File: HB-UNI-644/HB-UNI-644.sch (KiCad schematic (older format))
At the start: 49 parts, among them J1 FTDI, J10 ICSP, J11 RAW, J12 Conn_Gnd, J13 Conn_NTC, J2 GS2, J3 I2C_1, J4 GS2, J5 I2C_2, J6 I2C_3, J7 I2C_4, J8 Conn_A, J9 Conn_B, Q1 IRLML6244/IRLML0030, SW1 CONFIG, U1 ATMEGA644PA-AU, U2 CC1101, U3 MAX1724, U4 LM3480-3.3, Y1 8MHz

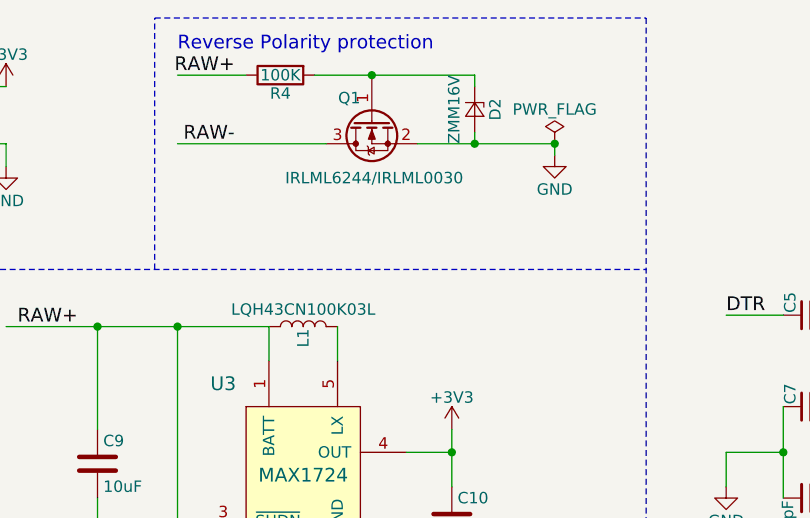
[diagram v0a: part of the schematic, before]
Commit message: Added hint to schematic which mosfet to use on HB-UNI-644
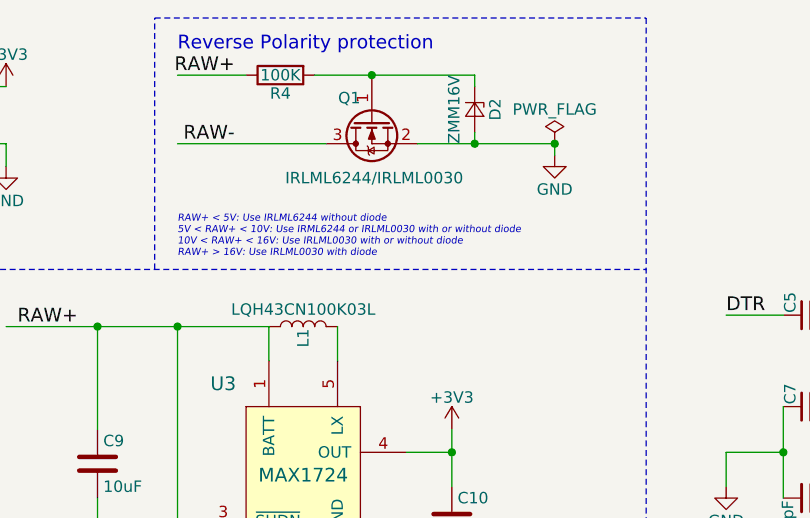
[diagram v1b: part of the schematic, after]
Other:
- note added: "RAW+ < 5V: Use IRLML6244 without diode\n5V < RAW+ < 10V: Use IRML6244 or IRLML0030 with or without diode\n10V < RAW+ < 16V: Use IRLML0030 with or without diode\nRAW+ > 16V: Use IRLML0030 with diode"
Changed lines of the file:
@@
 encoding utf-8
 Sheet 1 1
-Title ""
-Date ""
-Rev ""
-Comp ""
+Title "HB-UNI-644"
+Date "2018-06-17"
+Rev "1.1"
+Comp "Alexander Reinert"
 Comment1 ""
 Comment2 ""
@@
 Connection ~ 4650 3050
 Connection ~ 4150 3050
+Text Notes 3450 1600 0    31   Italic 0
+RAW+ < 5V: Use IRLML6244 without diode\n5V < RAW+ < 10V: Use IRML6244 or IRLML0030 with or without diode\n10V < RAW+ < 16V: Use IRLML0030 with or without diode\nRAW+ > 16V: Use IRLML0030 with diode
 $EndSCHEMATC

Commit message: Revision 2 of HB-UNI-644
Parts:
- removed J12: Conn_Gnd, Pin_Headers:Pin_Header_Straight_1x01_Pitch2.54mm, symbol Conn_01x01
- removed J8: Conn_A, Pin_Headers:Pin_Header_Straight_2x08_Pitch2.54mm, symbol Conn_02x08_Odd_Even
- removed J9: Conn_B, Pin_Headers:Pin_Header_Straight_2x08_Pitch2.54mm, symbol Conn_02x08_Odd_Even
- removed U4: LM3480-3.3, TO_SOT_Packages_SMD:SOT-23_Handsoldering, symbol LM3480-3.3
- added C15: 1000uF, Capacitors_THT:CP_Radial_D8.0mm_P3.50mm, symbol CP
- added C16, C18, C19: 10uF, Capacitors_SMD:C_0805_HandSoldering, symbol C_Small
- added C17, C20, C21: 10nF, Capacitors_SMD:C_0805_HandSoldering, symbol C_Small
- added F1: *, Resistors_SMD:R_1206_HandSoldering, symbol Polyfuse_Small
- added J12: Conn_01x04, Pin_Headers:Pin_Header_Straight_1x04_Pitch2.54mm, symbol Conn_01x04
- added J8: Conn_A, Pin_Headers:Pin_Header_Straight_2x09_Pitch2.54mm, symbol Conn_02x09_Odd_Even
- added J9: Conn_B, Pin_Headers:Pin_Header_Straight_2x09_Pitch2.54mm, symbol Conn_02x09_Odd_Even
- added Q2: IRLML5203, TO_SOT_Packages_SMD:SOT-23_Handsoldering, symbol Q_PMOS_GSD
- added Q3: IRF4905S, TO_SOT_Packages_SMD:TO-263-2, symbol Q_PMOS_GSD
- added R11, R12: 100K, Resistors_SMD:R_0805_HandSoldering, symbol R
- added U4: HT7533-1, TO_SOT_Packages_SMD:SOT-89-3_Handsoldering, symbol HT7533-1
- added U5: CC1101, Homebrew:CC1101, symbol CC1101
- added U6: LM3480-3.3, TO_SOT_Packages_SMD:SOT-23, symbol LM3480-3.3
- added U7: TXS0108EPWR, Housings_SSOP:TSSOP-20_4.4x6.5mm_Pitch0.65mm, symbol TXS0108EPWR
- C12, C9: footprint Capacitors_SMD:C_1206_HandSoldering -> Capacitors_SMD:C_0805_HandSoldering
- D2: value ZMM16V -> ZMM16
- Q1: value IRLML6244/IRLML0030 -> IRLML6244
- Y1: value 8MHz -> 8MHz/16MHz
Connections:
- net labels added: +3.3V, RAW+FUSE, VCC
- net labels removed: +3V3
- wire segments 187 -> 243
- no-connect marks 1 -> 8
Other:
- note added: "Battery holder"
- note added: "Battery voltage sensor"
- note added: "F1:\nPoweroption 1: PTC 6V/250mA\nPoweroption 2: PTC 16V/250mA\nPoweroption 3: PTC 30V/2A"
- note added: "J2:\nNeeds to be shortened for Poweroption 2 + 3"
- note added: "Power Option 2: Buck LDO (5-12V IN, 100mA)"
- note added: "Power Option 3: External MP2315 stepup PCB\n(5-24V IN, 1A)"
- note added: "Radio Module (VCC = 3.3V)"
- note added: "Radio Module (VCC = 5V)"
- note removed: "Power Option 2: Stepdown (5-24V IN)"
- note removed: "RAW+ < 5V: Use IRLML6244 without diode\n5V < RAW+ < 10V: Use IRML6244 or IRLML0030 with or without diode\n10V < RAW+ < 16V: Use IRLML0030 with or without diode\nRAW+ > 16V: Use IRLML0030 with diode"
- note removed: "Radio module"
- note removed: "Reverse Polarity protection"
- moved on the sheet: BT1, BT2, C1, C10, C11, C12, C13, C14, C2, C3, C4, C5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

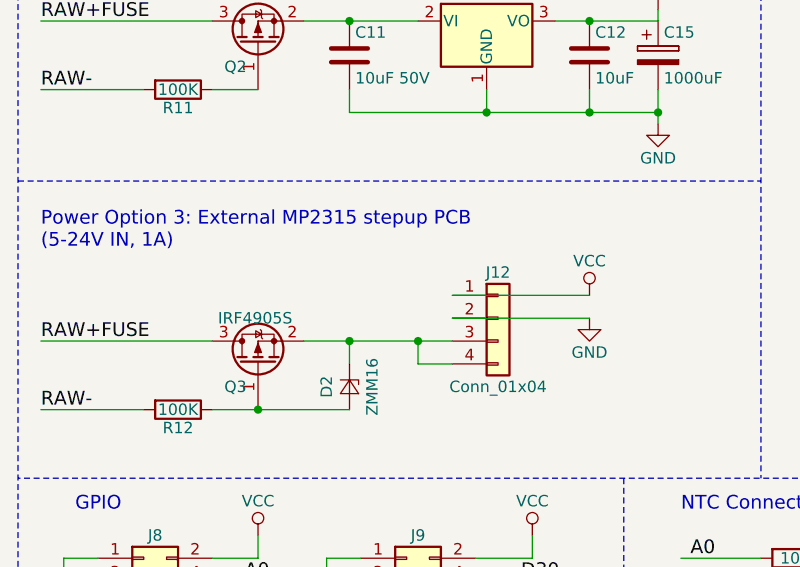
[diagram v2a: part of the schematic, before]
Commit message: Fixed Stepdown module on HB-UNI-644
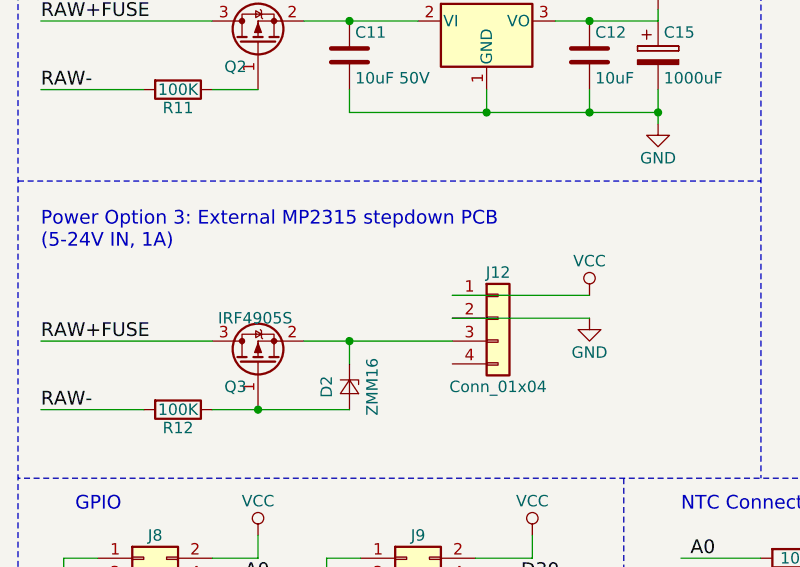
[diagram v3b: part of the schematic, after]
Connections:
- wire segments 243 -> 241
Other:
- note added: "Power Option 3: External MP2315 stepdown PCB\n(5-24V IN, 1A)"
- note removed: "Power Option 3: External MP2315 stepup PCB\n(5-24V IN, 1A)"
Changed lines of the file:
@@
 Sheet 1 1
 Title "HB-UNI-644"
-Date "2018-06-24"
-Rev "2.0"
+Date "2018-07-31"
+Rev "2.2"
 Comp "Alexander Reinert"
 Comment1 ""
@@
 Battery voltage sensor
 Text Notes 650  3850 0    60   ~ 0
-Power Option 3: External MP2315 stepup PCB\n(5-24V IN, 1A)
+Power Option 3: External MP2315 stepdown PCB\n(5-24V IN, 1A)
 $Comp
 L Conn_01x04 J12
@@
 	1800 4250 2450 4250
 Wire Wire Line
-	2300 4250 2300 4350
-Wire Wire Line
-	2300 4350 2450 4350
-Connection ~ 2300 4250
-Wire Wire Line
 	2450 4150 3050 4150

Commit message: * Switched to Kicad 5 * Added HB-UNI-644-S4-A4 addon Board
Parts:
- BT1, BT2: symbol Battery_Cell -> Device:Battery_Cell
- C1, C13, C14, C16, C17, C18, C19, C2, C20, C21, C3, C4, C5, C6, C7, C8: symbol C_Small -> Device:C_Small
- C10, C11, C12, C9: symbol C -> Device:C
- C15: symbol CP -> Device:CP
- D1: symbol LED_Dual_ACA -> Device:LED_Dual_ACA
- D2: symbol D_Zener_Small -> Device:D_Zener_Small
- F1: symbol Polyfuse_Small -> Device:Polyfuse_Small
- J1: symbol Conn_01x06 -> conn:Conn_01x06
- J10: symbol Conn_02x03_Odd_Even -> conn:Conn_02x03_Odd_Even
- J11, J13: symbol Conn_01x02 -> conn:Conn_01x02
- J12, J3, J5, J6, J7: symbol Conn_01x04 -> conn:Conn_01x04
- J2, J4: symbol GS2 -> conn:GS2
- J8, J9: symbol Conn_02x09_Odd_Even -> conn:Conn_02x09_Odd_Even
- L1: symbol L -> Device:L
- Q1: symbol Q_NMOS_GSD -> Device:Q_NMOS_GSD
- Q2, Q3: symbol Q_PMOS_GSD -> Device:Q_PMOS_GSD
- R1, R10, R11, R12, R2, R3, R4, R5, R6, R7, R8, R9: symbol R -> Device:R
- SW1: symbol SW_Push -> switches:SW_Push
- U1: symbol ATMEGA644PA-AU -> atmel:ATMEGA644PA-AU
- U2, U5: symbol CC1101 -> Homebrew:CC1101
- U3: symbol MAX1724-RESCUE-HB-UNI-644 -> HB-UNI-644-rescue:MAX1724-RESCUE-HB-UNI-644
- U4: symbol HT7533-1 -> Homebrew:HT7533-1
- U6: symbol LM3480-3.3 -> regul:LM3480-3.3
- U7: symbol TXS0108EPWR -> Homebrew:TXS0108EPWR
- Y1: symbol Crystal_Small -> Device:Crystal_Small
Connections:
- wire segments 241 -> 319
- no-connect marks 8 -> 9
